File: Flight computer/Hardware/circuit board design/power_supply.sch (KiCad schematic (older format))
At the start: 15 parts, among them J3 Conn_01x02, Q1 Q_PMOS_DGS, U9 TPS61200DRC

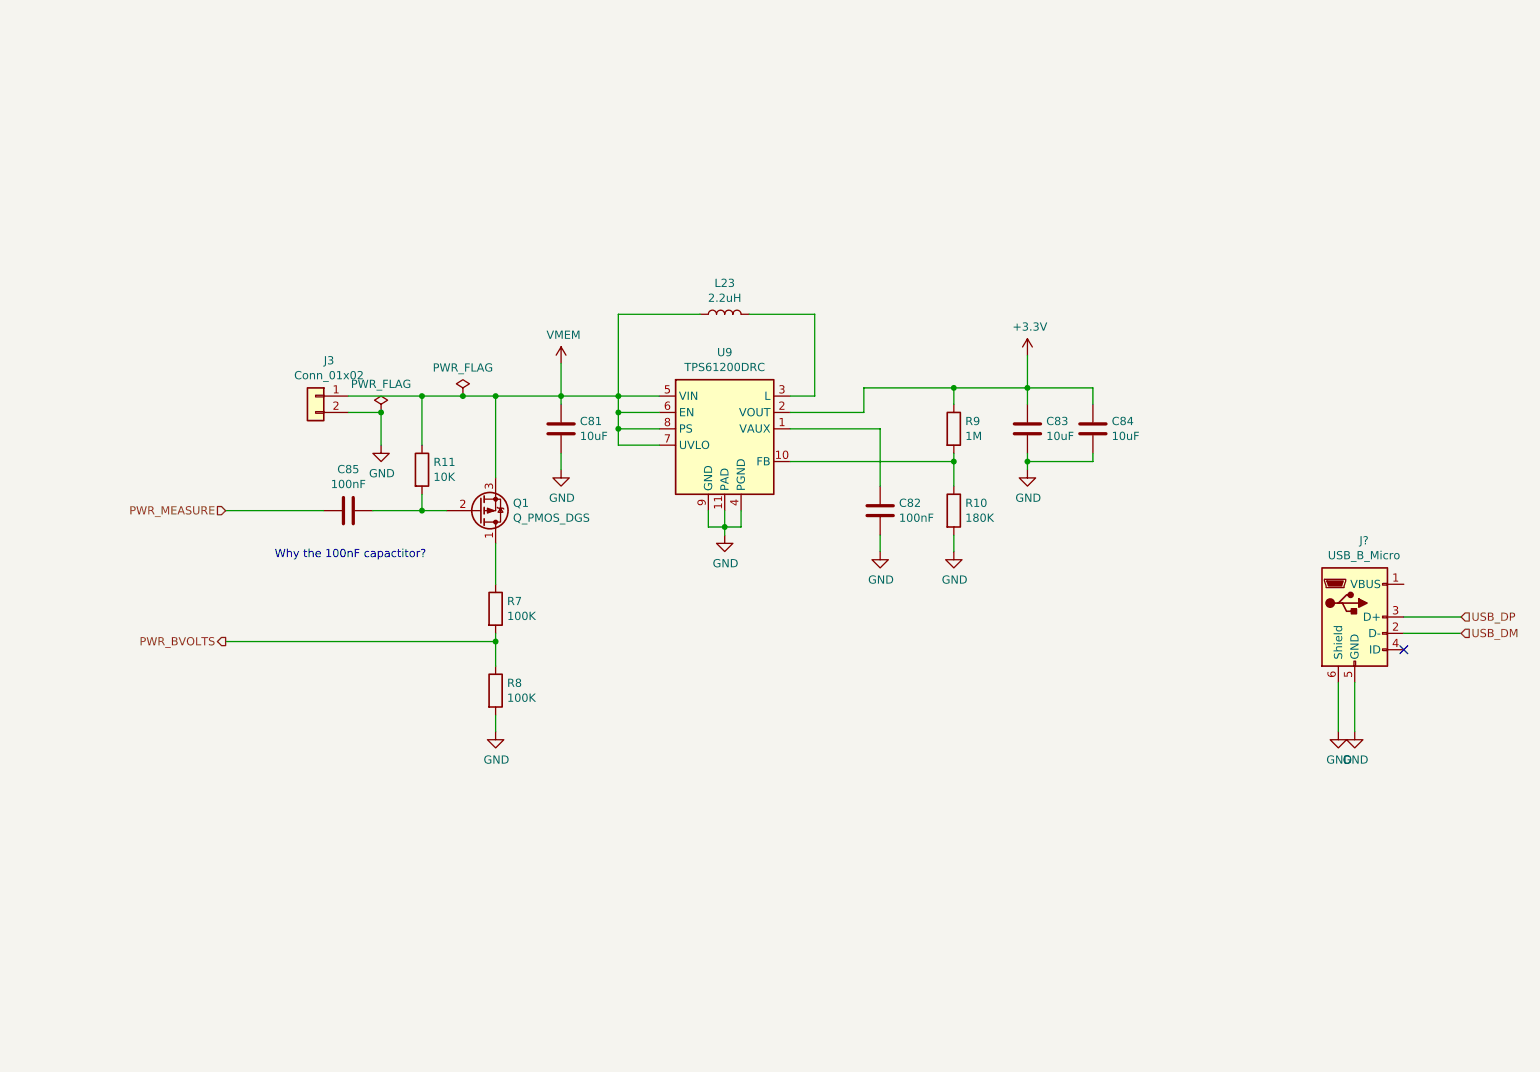
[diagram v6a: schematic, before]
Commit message: removed the 37khz crystal
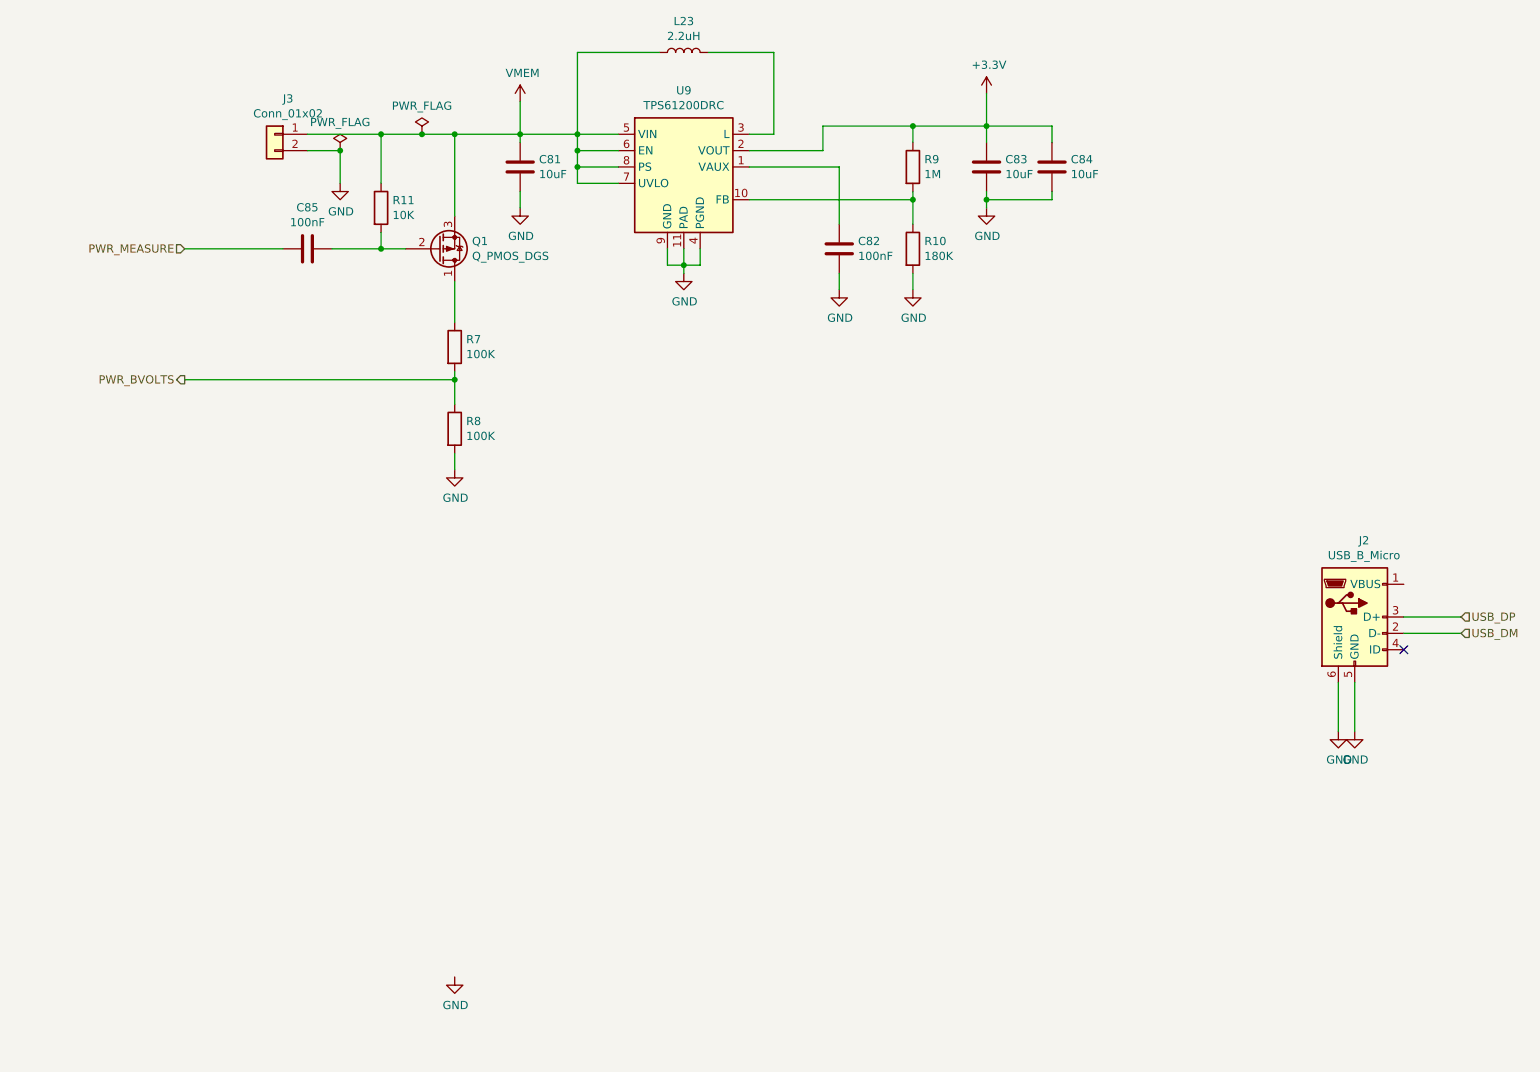
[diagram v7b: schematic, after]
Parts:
- U9: Cost (none) -> 1.91; Purchase link (none) -> https://www.mouser.co.uk/ProductDetail/Texas-Instruments/TP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
- gave numbers to parts that had none: 1
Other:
- note removed: "Why the 100nF capactitor?"
- moved on the sheet: C81, C82, C83, C84, C85, J3, L23, Q1, R10, R11, R7, R8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

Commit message: fixed errors with symbol and footprint connections
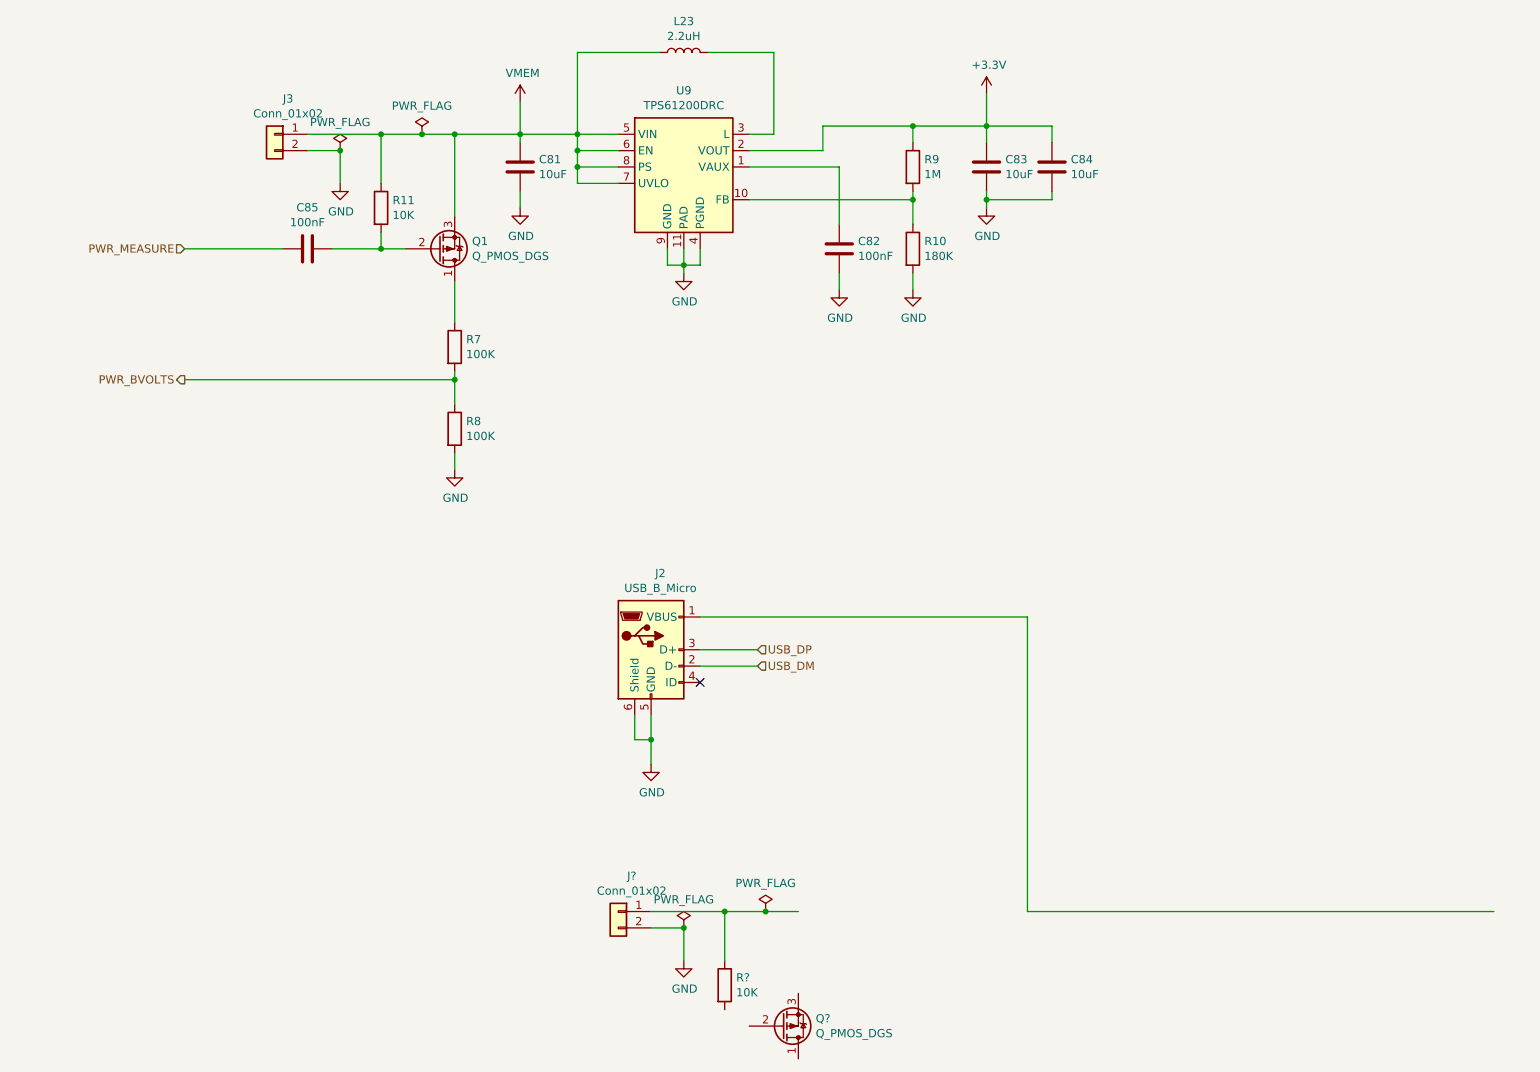
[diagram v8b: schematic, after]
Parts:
- added J?: Conn_01x02, Connector_PinHeader_1.00mm:PinHeader_1x02_P1.00mm_Vertical, symbol Connector_Generic:Conn_01x02
- added Q?: Q_PMOS_DGS, Package_TO_SOT_SMD:SOT-23, symbol Device:Q_PMOS_DGS
- added R?: 10K, Resistor_SMD:R_0603_1608Metric, symbol Device:R
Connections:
- wire segments 63 -> 74
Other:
- moved on the sheet: J2
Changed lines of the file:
@@
 Wire Wire Line
 	4150 1350 4150 1550
-NoConn ~ 9550 4700
-Wire Wire Line
-	9150 4900 9150 5200
-$Comp
-L power:GND #PWR?
-U 1 1 5D941F2E
-P 9150 5200
-AR Path="/5D5B15F7/5D941F2E" Ref="#PWR?"  Part="1"
-AR Path="/5D5B1705/5D941F2E" Ref="#PWR0103"  Part="1"
-F 0 "#PWR0103" H 9150 4950 50  0001 C CNN
-F 1 "GND" H 9155 5027 50  0000 C CNN
-F 2 "" H 9150 5200 50  0001 C CNN
-F 3 "" H 9150 5200 50  0001 C CNN
-	1    9150 5200
-	1    0    0    -1
-$EndComp
-Wire Wire Line
-	9250 4900 9250 5200
-Wire Wire Line
-	9900 4500 9550 4500
-Wire Wire Line
-	9550 4600 9900 4600
-$Comp
-L power:GND #PWR?
-U 1 1 5D941F37
-P 9250 5200
-AR Path="/5D5B15F7/5D941F37" Ref="#PWR?"  Part="1"
-AR Path="/5D5B1705/5D941F37" Ref="#PWR0104"  Part="1"
-F 0 "#PWR0104" H 9250 4950 50  0001 C CNN
-F 1 "GND" H 9255 5027 50  0000 C CNN
-F 2 "" H 9250 5200 50  0001 C CNN
-F 3 "" H 9250 5200 50  0001 C CNN
-	1    9250 5200
-	1    0    0    -1
-$EndComp
+NoConn ~ 5250 4900
+Wire Wire Line
+	4950 5100 4950 5250
+Wire Wire Line
+	5600 4700 5250 4700
+Wire Wire Line
+	5250 4800 5600 4800
 $Comp
 L Connector:USB_B_Micro J?
 U 1 1 5D941F3D
-P 9250 4500
+P 4950 4700
 AR Path="/5D5B15F7/5D941F3D" Ref="J?"  Part="1"
 AR Path="/5D5B1705/5D941F3D" Ref="J2"  Part="1"
-F 0 "J2" H 9307 4967 50  0000 C CNN
-F 1 "USB_B_Micro" H 9307 4876 50  0000 C CNN
-F 2 "Connector_USB:USB_Micro-B_Molex-105017-0001" H 9400 4450 50  0001 C CNN
-F 3 "~" H 9400 4450 50  0001 C CNN
-	1    9250 4500
-	1    0    0    -1
-$EndComp
-Text HLabel 9900 4600 2    50   Input ~ 0
+F 0 "J2" H 5007 5167 50  0000 C CNN
+F 1 "USB_B_Micro" H 5007 5076 50  0000 C CNN
+F 2 "Connector_USB:USB_Micro-B_Molex-105017-0001" H 5100 4650 50  0001 C CNN
+F 3 "~" H 5100 4650 50  0001 C CNN
+	1    4950 4700
+	1    0    0    -1
+$EndComp
+Text HLabel 5600 4800 2    50   Input ~ 0
 USB_DM
-Text HLabel 9900 4500 2    50   Input ~ 0
+Text HLabel 5600 4700 2    50   Input ~ 0
 USB_DP
 Wire Wire Line
@@
 $Comp
 L power:GND #PWR?
-U 1 1 5D9CC0D5
-P 3750 6700
-F 0 "#PWR?" H 3750 6450 50  0001 C CNN
-F 1 "GND" H 3755 6527 50  0000 C CNN
-F 2 "" H 3750 6700 50  0001 C CNN
-F 3 "" H 3750 6700 50  0001 C CNN
-	1    3750 6700
-	1    0    0    -1
-$EndComp
+U 1 1 5D941F37
+P 4950 5400
+AR Path="/5D5B15F7/5D941F37" Ref="#PWR?"  Part="1"
+AR Path="/5D5B1705/5D941F37" Ref="#PWR0104"  Part="1"
+F 0 "#PWR0104" H 4950 5150 50  0001 C CNN
+F 1 "GND" H 4955 5227 50  0000 C CNN
+F 2 "" H 4950 5400 50  0001 C CNN
+F 3 "" H 4950 5400 50  0001 C CNN
+	1    4950 5400
+	1    0    0    -1
+$EndComp
+Wire Wire Line
+	4850 5100 4850 5250
+Wire Wire Line
+	4850 5250 4950 5250
+Connection ~ 4950 5250
+Wire Wire Line
+	4950 5250 4950 5400
+Wire Wire Line
+	5250 4500 7250 4500
+Wire Wire Line
+	7250 4500 7250 6300
+Wire Wire Line
+	7250 6300 10100 6300
+$Comp
+L power:GND #PWR?
+U 1 1 5D79E558
+P 5150 6600
+F 0 "#PWR?" H 5150 6350 50  0001 C CNN
+F 1 "GND" H 5155 6427 50  0000 C CNN
+F 2 "" H 5150 6600 50  0001 C CNN
+F 3 "" H 5150 6600 50  0001 C CNN
+	1    5150 6600
+	1    0    0    -1
+$EndComp
+$Comp
+L Connector_Generic:Conn_01x02 J?
+U 1 1 5D79E562
+P 4750 6300
+F 0 "J?" H 4668 6517 50  0000 C CNN
+F 1 "Conn_01x02" H 4668 6426 50  0000 C CNN
+F 2 "Connector_PinHeader_1.00mm:PinHeader_1x02_P1.00mm_Vertical" H 4750 6300 50  0001 C CNN
+F 3 "~" H 4750 6300 50  0001 C CNN
+	1    4750 6300
+	-1   0    0    -1
+$EndComp
+Wire Wire Line
+	5150 6600 5150 6400
+Wire Wire Line
+	5150 6400 4950 6400
+Wire Wire Line
+	4950 6300 5400 6300
+$Comp
+L Device:R R?
+U 1 1 5D79E56F
+P 5400 6750
+F 0 "R?" H 5470 6796 50  0000 L CNN
+F 1 "10K" H 5470 6705 50  0000 L CNN
+F 2 "Resistor_SMD:R_0603_1608Metric" V 5330 6750 50  0001 C CNN
+F 3 "~" H 5400 6750 50  0001 C CNN
+	1    5400 6750
+	1    0    0    -1
+$EndComp
+$Comp
+L Device:Q_PMOS_DGS Q?
+U 1 1 5D79E579
+P 5750 7000
+F 0 "Q?" H 5956 6954 50  0000 L CNN
+F 1 "Q_PMOS_DGS" H 5956 7045 50  0000 L CNN
+F 2 "Package_TO_SOT_SMD:SOT-23" H 5950 7100 50  0001 C CNN
+F 3 "~" H 5750 7000 50  0001 C CNN
+	1    5750 7000
+	1    0    0    1
+$EndComp
+Wire Wire Line
+	5400 6600 5400 6300
+Connection ~ 5400 6300
+Wire Wire Line
+	5400 6300 5650 6300
+$Comp
+L power:PWR_FLAG #FLG?
+U 1 1 5D79E586
+P 5650 6300
+F 0 "#FLG?" H 5650 6375 50  0001 C CNN
+F 1 "PWR_FLAG" H 5650 6473 50  0000 C CNN
+F 2 "" H 5650 6300 50  0001 C CNN
+F 3 "~" H 5650 6300 50  0001 C CNN
+	1    5650 6300
+	1    0    0    -1
+$EndComp
+Connection ~ 5650 6300
+Wire Wire Line
+	5650 6300 5850 6300
+$Comp
+L power:PWR_FLAG #FLG?
+U 1 1 5D79E592
+P 5150 6400
+F 0 "#FLG?" H 5150 6475 50  0001 C CNN
+F 1 "PWR_FLAG" H 5150 6573 50  0000 C CNN
+F 2 "" H 5150 6400 50  0001 C CNN
+F 3 "~" H 5150 6400 50  0001 C CNN
+	1    5150 6400
+	1    0    0    -1
+$EndComp
+Connection ~ 5150 6400
 $EndSCHEMATC
